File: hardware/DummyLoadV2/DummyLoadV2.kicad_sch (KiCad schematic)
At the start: 7 parts, among them Q1 FQP30N06L, U1 MAX4167

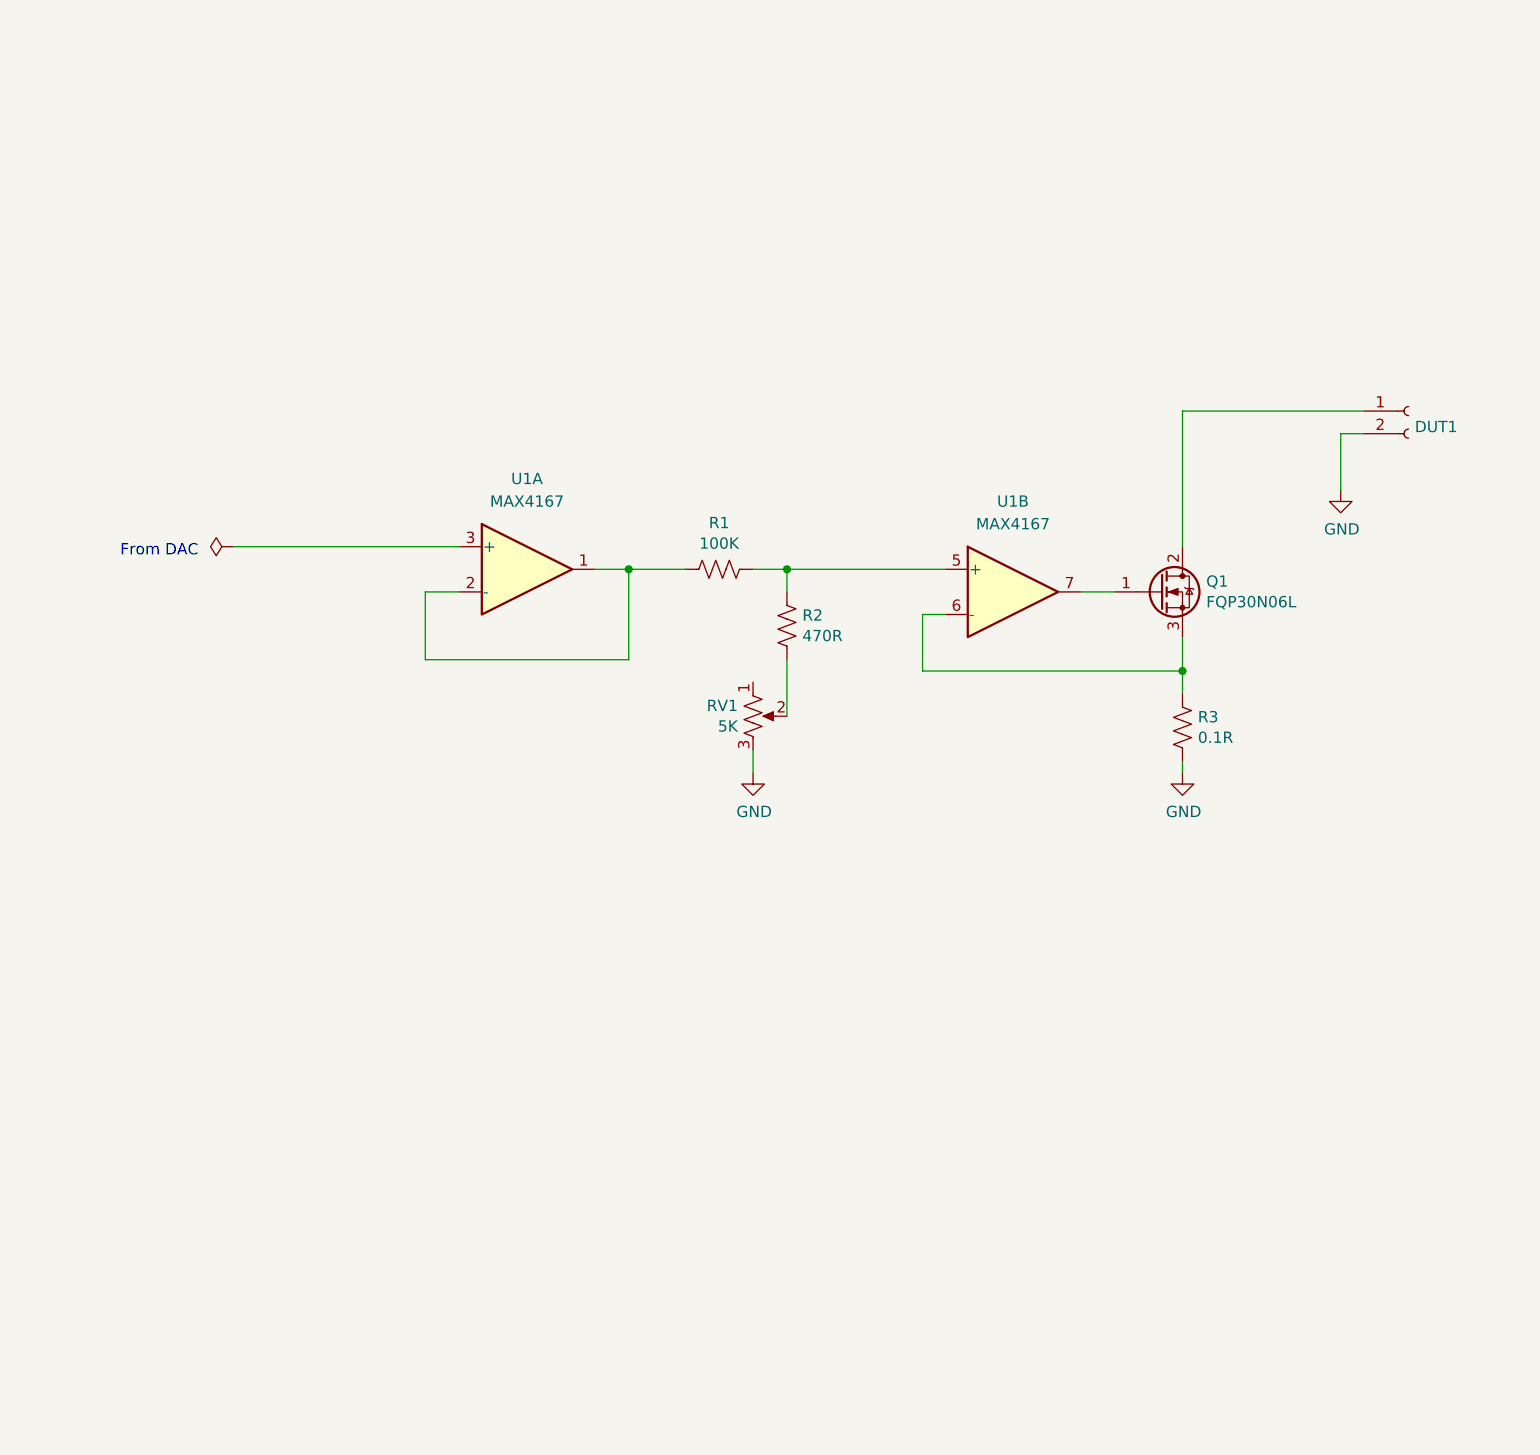
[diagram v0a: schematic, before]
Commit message: Moved pins around
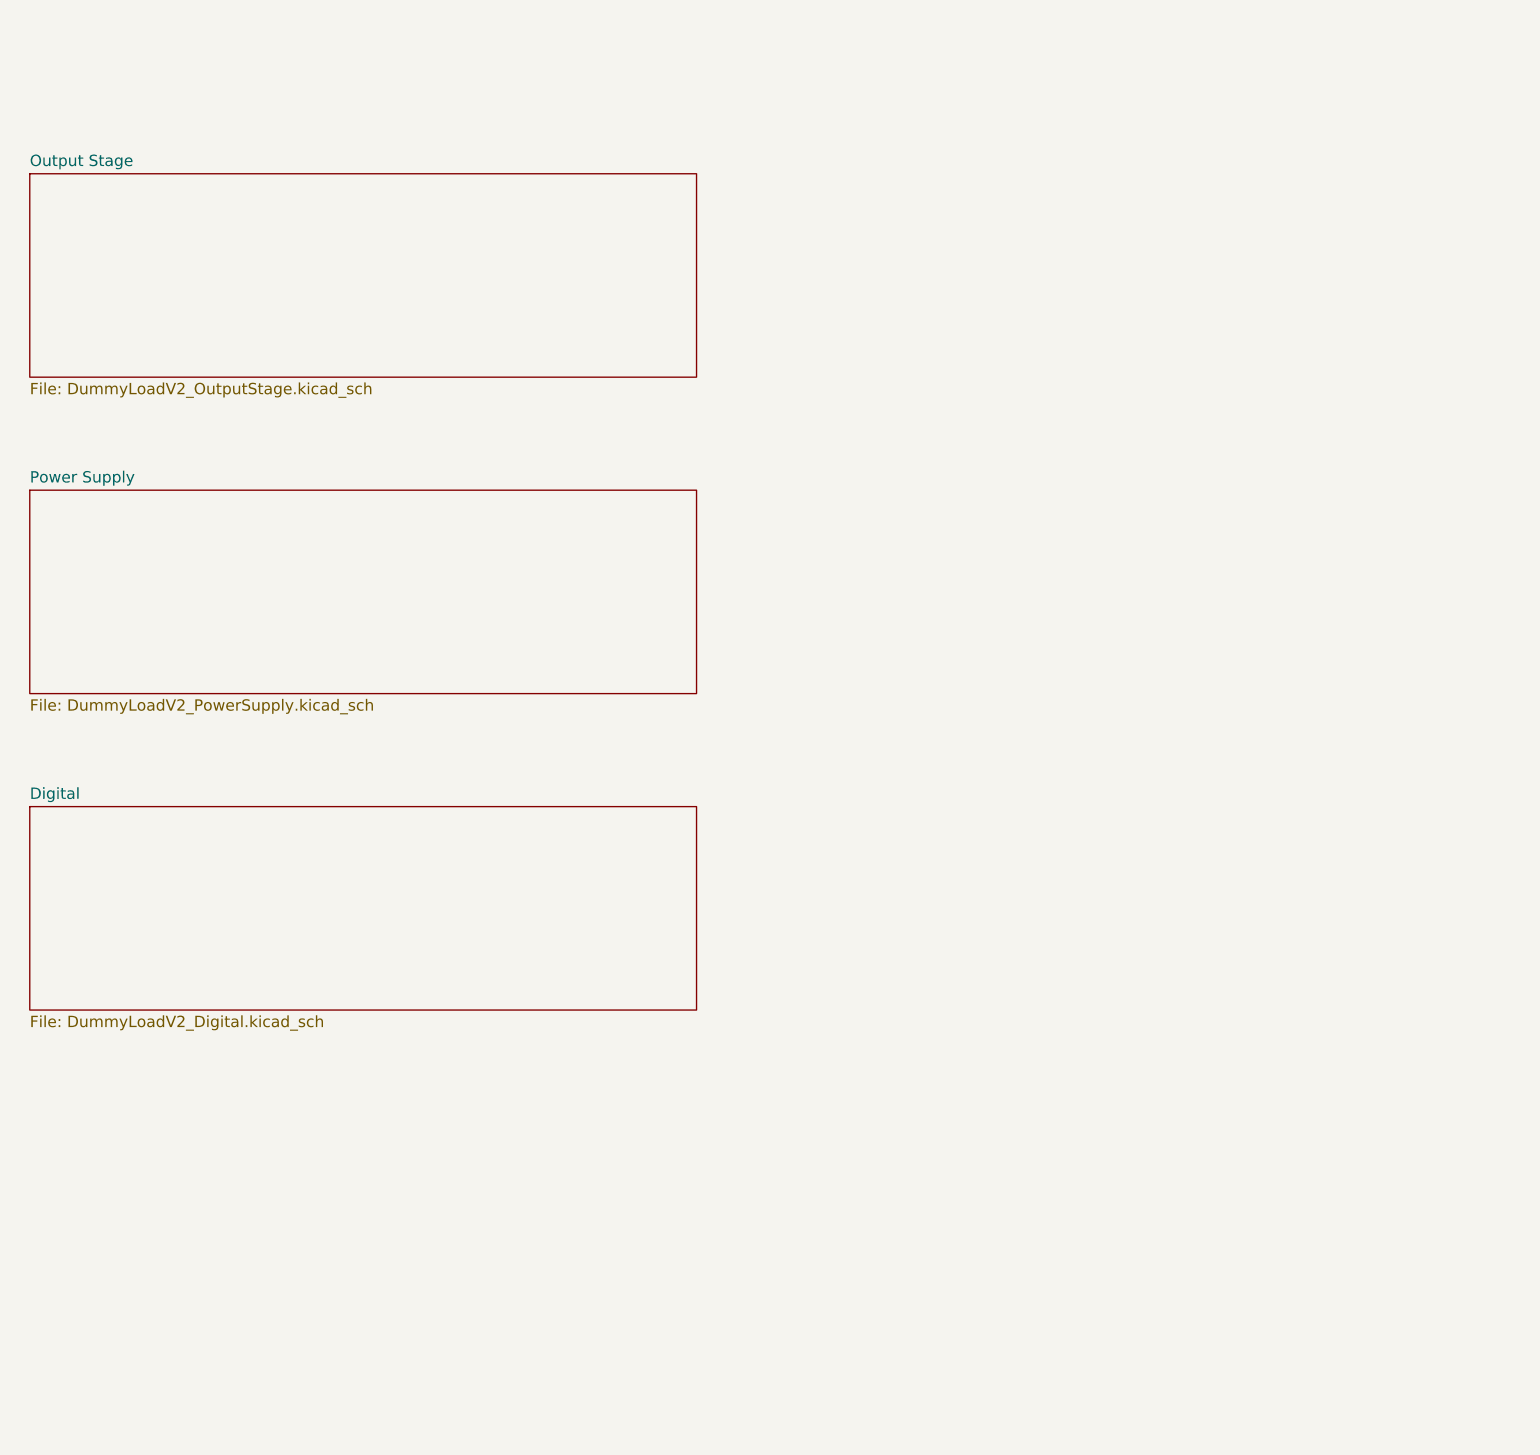
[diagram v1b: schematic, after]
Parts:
- removed DUT1: Conn_01x02_Female, symbol BasicDummyLoad-rescue:Conn_01x02_Female-Connector
- removed Q1: FQP30N06L, Package_TO_SOT_SMD:TO-252-2, symbol Transistor_FET:QM6006D
- removed R1: 100K, symbol Device:R_US
- removed R2: 470R, symbol Device:R_US
- removed R3: 0.1R, symbol Device:R_US
- removed RV1: 5K, symbol BasicDummyLoad-rescue:R_POT_US-Device
- removed U1: MAX4167, symbol Amplifier_Operational:TL062
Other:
- added sheet Digital (DummyLoadV2_Digital.kicad_sch)
- added sheet Output Stage (DummyLoadV2_OutputStage.kicad_sch)
- added sheet Power Supply (DummyLoadV2_PowerSupply.kicad_sch)
- note removed: "From DAC"

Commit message: Updated schematic
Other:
- sheet Output Stage renamed Analog
- removed sheet Power Supply
- sheet Analog: file DummyLoadV2_OutputStage.kicad_sch -> DummyLoadV2_Analog.kicad_sch
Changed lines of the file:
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@@
     (rev "1")
   )
-  (sheet (at 57.15 109.22) (size 74.93 22.86) (fields_autoplaced)
+  (sheet (at 55.88 78.74) (size 74.93 22.86) (fields_autoplaced)
     (stroke (width 0.1524) (type solid))
     (fill (color 0 0 0 0.0000))
-    (property "Sheetname" "Digital" (at 57.15 108.5084 0)
+    (property "Sheetname" "Digital" (at 55.88 78.0284 0)
       (effects (font (size 1.27 1.27)) (justify left bottom))
     )
-    (property "Sheetfile" "DummyLoadV2_Digital.kicad_sch" (at 57.15 132.6646 0)
+    (property "Sheetfile" "DummyLoadV2_Digital.kicad_sch" (at 55.88 102.1846 0)
       (effects (font (size 1.27 1.27)) (justify left top))
     )
@@
     )
   )
-  (sheet (at 57.15 73.66) (size 74.93 22.86) (fields_autoplaced)
+  (sheet (at 56.515 38.1) (size 74.93 22.86) (fields_autoplaced)
     (stroke (width 0.1524) (type solid))
     (fill (color 0 0 0 0.0000))
-    (property "Sheetname" "Power Supply" (at 57.15 72.9484 0)
+    (property "Sheetname" "Analog" (at 56.515 37.3884 0)
       (effects (font (size 1.27 1.27)) (justify left bottom))
     )
-    (property "Sheetfile" "DummyLoadV2_PowerSupply.kicad_sch" (at 57.15 97.1046 0)
+    (property "Sheetfile" "DummyLoadV2_Analog.kicad_sch" (at 56.515 61.5446 0)
       (effects (font (size 1.27 1.27)) (justify left top))
     )
-    (instances
-      (project "DummyLoadV2"
-        (path "/154f9743-c032-4045-ba5f-d157ba47940d" (page "3"))
-      )
-    )
-  )
-  (sheet (at 57.15 38.1) (size 74.93 22.86) (fields_autoplaced)
-    (stroke (width 0.1524) (type solid))
-    (fill (color 0 0 0 0.0000))
-    (property "Sheetname" "Output Stage" (at 57.15 37.3884 0)
-      (effects (font (size 1.27 1.27)) (justify left bottom))
-    )
-    (property "Sheetfile" "DummyLoadV2_OutputStage.kicad_sch" (at 57.15 61.5446 0)
-      (effects (font (size 1.27 1.27)) (justify left top))
-    )

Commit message: Updated schematic
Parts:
- added C1 (x2), C10: 0.1uF, symbol Device:C_Small
- added C11: 10uF, symbol Device:C_Small
- added C13 (x2): 100uF, symbol Device:C_Polarized_Small
- added C2 (x2): 22uF, symbol Device:C_Small
- added D1 (x2): LED, symbol Device:LED
- added D5: 1N4001, Diode_THT:D_DO-41_SOD81_P10.16mm_Horizontal, symbol Diode:1N4001
- added J5 (x2): Power_A, symbol Connector_Generic:Conn_01x02
- added J5: Power_In, symbol Connector_Generic:Conn_01x02
- added R12, R22, R23: 1K, symbol Device:R_US
- added R5: 470R, symbol Device:R_US
- added SW2: SW_SPST_LED, symbol Switch:SW_SPST_LED
- added U2: LM4040-4.1, Package_TO_SOT_THT:TO-92_Inline, symbol Reference_Voltage:LM4040LP-4.1
- added U7: R-78E-0.5, Package_TO_SOT_THT:TO-92_Inline, symbol Regulator_Linear:L78L05_TO92
- added U7: L78L05, Package_TO_SOT_THT:TO-92_Inline, symbol Regulator_Linear:L78L05_TO92
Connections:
- new net: D1.1 (K), R22.2
- new net: D5.1 (K), SW2.1
- new net: D5.2 (A), J5.1 (Pin_1)
- new net: R23.2, SW2.4 (A)
- new net: D1.1 (K), R12.2
- new net +12V: C13.1, C13.1, D1.2 (A), D1.2 (A), J5.1 (Pin_1), J5.1 (Pin_1), SW2.2, U7.3 (VI), U7.3 (VI)
- new net GNDA: C1.2, C1.2, C10.2, C11.2, C13.2, C13.2, C2.2, C2.2, J5.2 (Pin_2), J5.2 (Pin_2), J5.2 (Pin_2), R12.1, R22.1, SW2.3 (K), U2.3 (A), U7.2 (GND), U7.2 (GND)
- new net VDD: C1.1, C2.1, R23.1, U7.1 (VO)
- new net VDDA: C1.1, C2.1, R5.2, U7.1 (VO)
- new net VREF: C10.1, C11.1, R5.1, U2.2 (K)
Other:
- note added: "Notes: Switch LED VCC from FP LED VCC"
